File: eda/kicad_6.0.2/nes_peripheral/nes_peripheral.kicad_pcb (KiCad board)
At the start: 2 copper layers, 100 x 100 mm, 119 parts, among them J1 CONN_USER, J10 CONN_JOY2, J11 CONN_JOY2_OE_SEL, J12 CONN_JOY1_OE_SEL, J15 CONN_JOY1_MIC, J16 CONN_5V_RESERVE, J19 CONN_SOUND_IO, J2 CONN_JOY1_FC_COMPATIBLE, J22 CONN_JOY2_MIC, J23 FC_CONN, J24 CONN_CART_DBG, J25 CONN_CART_DBG, J28 CONN_JOY2_DBGSEL, J29 CONN_JOY1_DBGSEL, J3 CONN_JOY2_FC_COMPATIBLE, J30 CONN_GAINSEL, J31 Screw_Terminal_SPK, J32 CONN_SPK, J33 CONN_JOY2_DBG, J34 CONN_JOY1_DBG, J4 Jack_EXT5V, J7 CONN_CART_OE_SEL, J8 CONN_5VSEL, J9 CONN_JOY1, U1 TXB0104PW, U10 TXB0104PW, U11 TXB0104PW, U12 TXB0104PW, U13 TXB0104PW, U14 TXB0104PW, U15 TXB0104PW, U16 TXB0104PW, U17 4021, U18 4021, U19 MAX98357, U2 TXB0104PW, U20 MAX98357, U3 TXB0104PW, U4 TXB0104PW, U5 TXB0104PW, U6 TXB0104PW, U7 TXB0104PW, U8 TXB0104PW, U9 TXB0104PW

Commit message: feat: レベル変換回路配線中
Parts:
- removed J19: CONN_SOUND_IO, Connector_PinSocket_2.54mm:PinSocket_2x03_P2.54mm_Vertical
- C1, C10, C14, C15, C18, C19, C2, C22, C23, C25, C26, C29, C30, C5, C6, C9, J16, J24, J25: moved to B.Cu
- U5: moved to F.Cu
- moved U6 223.4 mm to (96.5, 68.6)
- moved U13 214.4 mm to (96.5, 59.7)
- moved U3 199.0 mm to (83.8, 80.0)
- moved U14 195.0 mm to (96.5, 77.5)
- moved C6 193.0 mm to (85.9, 60.3), turned to 180 degrees
- moved U11 190.2 mm to (83.8, 71.1)
- moved U2 190.1 mm to (83.8, 62.2)
- moved C2 176.8 mm to (81.7, 60.3)
- moved U10 174.2 mm to (109.2, 57.1)
- moved C19 170.8 mm to (81.7, 69.2)
- moved C29 162.6 mm to (98.6, 57.8), turned to 180 degrees
- moved C23 160.4 mm to (85.9, 69.2), turned to 180 degrees
- moved C9 154.6 mm to (94.4, 48.9)
- moved C1 154.4 mm to (107.1, 46.3)
- moved C15 153.9 mm to (98.6, 66.7), turned to 180 degrees
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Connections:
- U14 pad 10: /3V3_~{PA13} -> /5V_~{PA13}
- U15 pad 10: /3V3_PD7 -> /5V_PD7
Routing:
- net GND: track 0.00 -> 1701.2 mm, vias 0 -> 256
- net +5V: track 0.00 -> 74.7 mm, vias 0 -> 8
- net /3V3_A6: track 0.00 -> 73.7 mm, vias 0 -> 2
- net /3V3_A7: track 0.00 -> 72.7 mm, vias 0 -> 2
- net /3V3_D6: track 0.00 -> 71.2 mm, vias 0 -> 2
- net /3V3_D7: track 0.00 -> 70.2 mm, vias 0 -> 2
- net +3V3: track 0.00 -> 70.0 mm, vias 0 -> 8
- net /3V3_A10: track 0.00 -> 67.2 mm
- net /3V3_A11: track 0.00 -> 66.3 mm
- net /5V_D2: track 0.00 -> 65.8 mm
- net /5V_~{WE}: track 0.00 -> 65.1 mm
- net /5V_D3: track 0.00 -> 64.9 mm
- net /3V3_A12: track 0.00 -> 64.6 mm
- net /BOARD_5V: track 0.00 -> 63.9 mm
- net /3V3_O2: track 0.00 -> 63.7 mm
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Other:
- outline, holes or cut-outs redrawn

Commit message: feat: レベル変換回路を引ききった
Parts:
- C11, C12, C16, C17, C20, C24, C27, C3, C31, C4, C7, C8: moved to B.Cu
- moved U12 228.4 mm to (83.8, 88.9)
- moved U8 205.7 mm to (96.5, 104.1)
- moved U7 204.4 mm to (96.5, 86.4)
- moved C3 200.8 mm to (81.7, 78.1)
- moved U15 186.5 mm to (96.5, 95.2)
- moved U4 173.9 mm to (83.8, 97.8)
- moved C16 172.8 mm to (98.6, 84.5), turned to 180 degrees
- moved C27 166.5 mm to (94.5, 93.4)
- moved C24 164.1 mm to (85.9, 87.0), turned to 180 degrees
- moved C11 162.7 mm to (94.5, 84.5)
- moved C8 161.9 mm to (85.9, 95.9), turned to 180 degrees
- moved C4 160.6 mm to (81.8, 95.9)
- moved C20 142.7 mm to (81.7, 87.0)
- moved C17 141.7 mm to (98.6, 102.3), turned to 180 degrees
- moved C31 141.5 mm to (98.6, 93.4), turned to 180 degrees
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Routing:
- net GND: track 1701.2 -> 2673.8 mm, vias 256 -> 322
- net +3V3: track 70.0 -> 182.6 mm, vias 8 -> 14
- net /5V_PA12: track 0.00 -> 70.4 mm
- net /5V_PA11: track 0.00 -> 69.8 mm
- net /5V_PD5: track 0.00 -> 69.2 mm
- net /5V_PD6: track 0.00 -> 68.6 mm
- net /5V_PA8: track 0.00 -> 68.0 mm
- net /CART_OE: track 61.6 -> 129.3 mm, vias 8 -> 14
- net /5V_PA7: track 0.00 -> 67.4 mm
- net +5V: track 74.7 -> 141.3 mm, vias 8 -> 14
- net /3V3_PA5: track 0.00 -> 62.7 mm, vias 0 -> 2
- net /3V3_PA6: track 0.00 -> 62.4 mm, vias 0 -> 2
- net /3V3_PA12: track 0.00 -> 61.3 mm, vias 0 -> 2
- net /3V3_PA1: track 0.00 -> 61.1 mm, vias 0 -> 2
- net /3V3_PA8: track 0.00 -> 60.5 mm, vias 0 -> 2
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
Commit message: feat: 残りの部品配置を修正中
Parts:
- removed J32: CONN_SPK, Resistor_SMD:R_0603_1608Metric_Pad0.98x0.95mm_HandSolder
- J11, J12, J7, J8: footprint Connector_PinSocket_2.54mm:PinSocket_1x03_P2.54mm_Vertical -> Connector_PinHeader_2.54mm:PinHeader_1x03_P2.54mm_Vertical
- J15, J22: footprint Connector_PinSocket_2.54mm:PinSocket_2x01_P2.54mm_Vertical -> Connector_PinSocket_2.54mm:PinSocket_1x02_P2.54mm_Vertical
- J28, J29: footprint Connector_PinSocket_2.54mm:PinSocket_2x01_P2.54mm_Vertical -> Connector_PinHeader_2.54mm:PinHeader_1x02_P2.54mm_Vertical
- J30: footprint Connector_PinSocket_2.54mm:PinSocket_2x05_P2.54mm_Vertical -> Connector_PinHeader_2.54mm:PinHeader_2x05_P2.54mm_Vertical
- J33, J34: footprint Resistor_SMD:R_0603_1608Metric_Pad0.98x0.95mm_HandSolder -> Connector_PinSocket_2.54mm:PinSocket_2x07_P2.54mm_Vertical
- moved U9 238.9 mm to (73.7, 113.0)
- moved U19 225.6 mm to (53.3, 114.3)
- moved U16 222.6 mm to (73.7, 120.7)
- moved J34 221.3 mm to (63.5, 137.2), turned to 90 degrees
- moved D1 215.5 mm to (83.6, 169.8)
- moved C21 215.5 mm to (72.9, 168.3)
- moved R15 215.5 mm to (72.9, 158.7)
- moved D2 215.5 mm to (78.3, 175.1)
- moved U20 212.6 mm to (61.0, 114.3)
- moved R23 204.9 mm to (50.8, 113.0), turned to -90 degrees
- moved U18 202.0 mm to (58.4, 129.5), turned to 90 degrees
- moved C28 201.8 mm to (31.6, 177.1)
- moved C35 201.8 mm to (20.1, 182.8)
- moved C36 201.8 mm to (46.1, 170.2)
- moved R11 201.8 mm to (20.1, 190.3)
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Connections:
- J15 pad 2: Net-(J15-Pad2) -> GND
- J22 pad 2: Net-(J22-Pad2) -> GND
- J33 pad 1: /JOY2_3V3_DBG_D0 -> /JOY2_3V3_DBG_D7
- J34 pad 1: /JOY1_3V3_DBG_D0 -> /JOY1_3V3_DBG_D7
- U16 pad 10: Net-(J22-Pad2) -> /5V_JOY2_MICIN
- U9 pad 10: Net-(J15-Pad2) -> /5V_JOY1_RESERVE
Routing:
- net /BOARD_5V: track 63.9 -> 21.8 mm
- net +3V3: track 182.6 -> 144.6 mm
- net GND: track 2673.8 -> 2675.8 mm, vias 322 -> 326

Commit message: wip: 電源配線中
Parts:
- J33, J34: footprint Connector_PinSocket_2.54mm:PinSocket_2x07_P2.54mm_Vertical -> Connector_PinSocket_2.54mm:PinSocket_2x09_P2.54mm_Vertical
- moved C39 15.8 mm to (62.6, 106.7)
- moved C38 11.0 mm to (62.6, 109.2)
- moved R24 9.24 mm to (57.1, 115.2)
- moved F1 1.04 mm to (106.6, 128.5), turned to -90 degrees
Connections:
- J8 pad 1: /BOARD_5V -> /EXT_5V
- J8 pad 3: /EXT_5V -> /BOARD_5V
- JP1 pad 11: /BOARD_5V -> unconnected-(JP1-Pad11)
- JP1 pad 29: +3V3 -> unconnected-(JP1-Pad29)
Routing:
- net GND: track 2675.8 -> 3019.4 mm, vias 326 -> 402
- net +5V: track 141.3 -> 216.6 mm, vias 14 -> 19
- net /BOARD_5V: track 21.8 -> 90.4 mm, vias 0 -> 4
- net +3V3: track 144.6 -> 207.7 mm, vias 14 -> 18
- net /DAC_I2S_BCLK: track 0.00 -> 34.6 mm, vias 0 -> 1
- net /DAC_I2S_DIN: track 0.00 -> 32.1 mm, vias 0 -> 1
- net /DAC_I2S_LRCLK: track 0.00 -> 31.6 mm, vias 0 -> 1
- net /DAC_~{SD_MODE}: track 0.00 -> 30.2 mm, vias 0 -> 1
- net /GPIO_0_D20: track 0.00 -> 28.1 mm, vias 0 -> 1
- net /GPIO_0_D21: track 0.00 -> 25.6 mm, vias 0 -> 1
- net /CART_OE_IN: track 0.00 -> 25.2 mm, vias 0 -> 1
- net /GPIO_0_D23: track 0.00 -> 23.8 mm, vias 0 -> 1
- net /EXT_5V: track 0.00 -> 15.0 mm, vias 0 -> 2
- net /3V3_PD5: track 55.6 -> 42.0 mm
- net /3V3_PA8: track 60.5 -> 51.2 mm
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
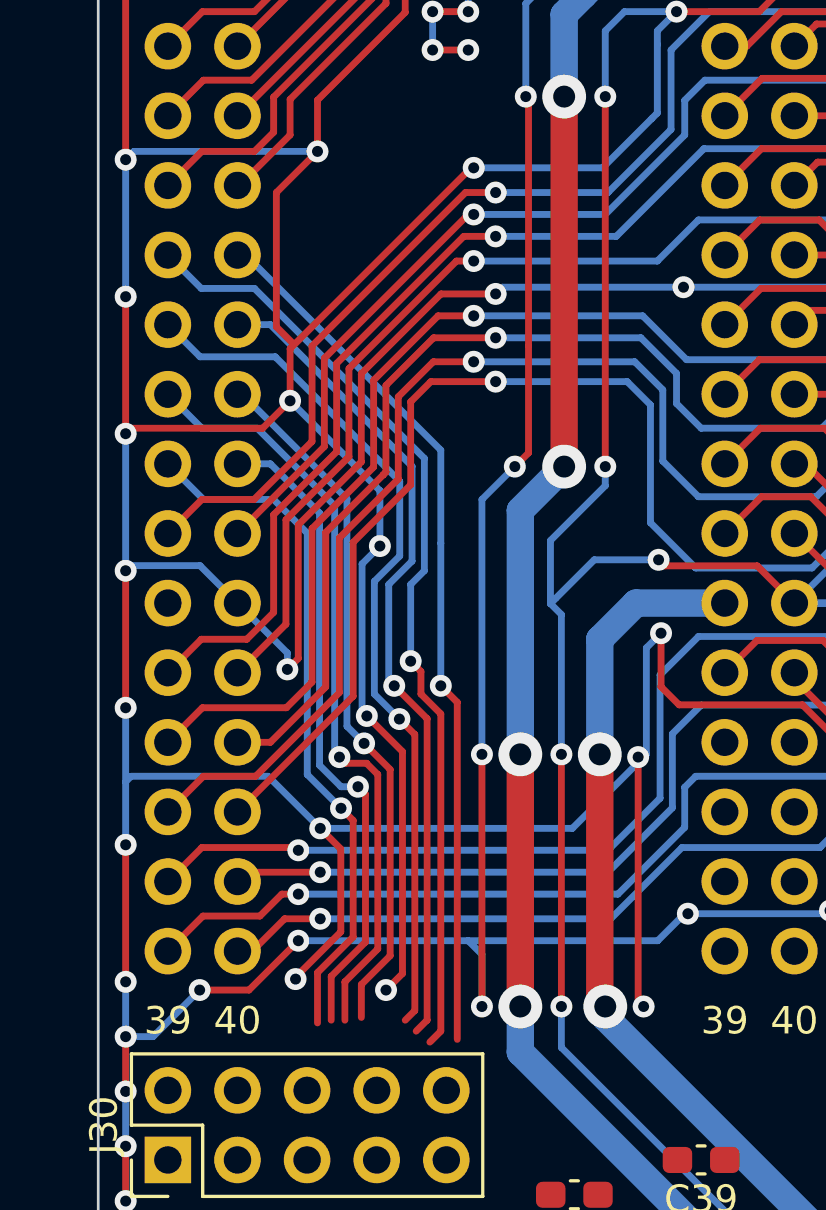
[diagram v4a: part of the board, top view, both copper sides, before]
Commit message: fix: I2Sのピン配置を変更
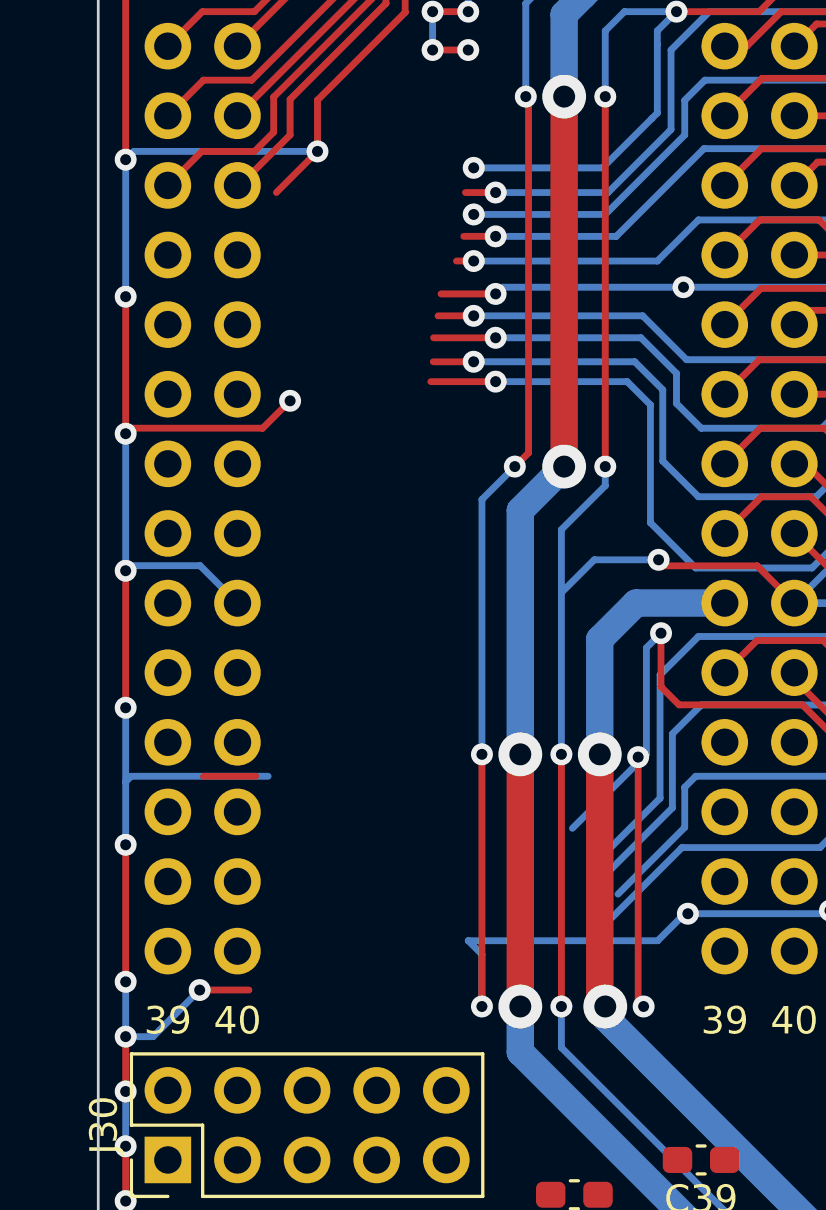
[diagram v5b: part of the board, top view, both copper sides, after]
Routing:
- net GND: track 3019.4 -> 2931.2 mm, vias 402 -> 395
- net /DAC_I2S_BCLK: track 34.6 -> 0.00 mm, vias 1 -> 0
- net /DAC_I2S_DIN: track 32.1 -> 0.30 mm, vias 1 -> 0
- net /DAC_I2S_LRCLK: track 31.6 -> 0.00 mm, vias 1 -> 0
- net /DAC_~{SD_MODE}: track 30.2 -> 0.00 mm, vias 1 -> 0
- net /GPIO_0_D20: track 28.1 -> 0.00 mm, vias 1 -> 0
- net /GPIO_0_D21: track 25.6 -> 0.18 mm, vias 1 -> 0
- net /CART_OE_IN: track 25.2 -> 0.00 mm, vias 1 -> 0
- net /GPIO_0_D23: track 23.8 -> 0.00 mm, vias 1 -> 0
- net /3V3_PA2: track 55.2 -> 33.8 mm
- net /3V3_PA5: track 54.8 -> 33.4 mm
- net /3V3_PA1: track 60.6 -> 40.9 mm
- net /3V3_PA12: track 61.1 -> 42.5 mm
- net /3V3_PA11: track 54.3 -> 35.9 mm
- net /3V3_PA8: track 51.2 -> 32.9 mm
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
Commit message: feat: コントローラの3V3パラレル配線を追加
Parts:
- C35, C36, R10, R11, R12, R13, R14, R15, R16, R17, R18, R19, R20, R21, R22, R7, R8, R9: moved to B.Cu
- J1: footprint Connector_PinSocket_2.54mm:PinSocket_1x06_P2.54mm_Vertical -> Connector_PinSocket_2.54mm:PinSocket_1x04_P2.54mm_Vertical
- J33, J34: footprint Connector_PinSocket_2.54mm:PinSocket_2x09_P2.54mm_Vertical -> Connector_PinSocket_2.54mm:PinSocket_1x09_P2.54mm_Vertical
- moved R11 86.9 mm to (70.9, 119.9), turned to -90 degrees
- moved R7 82.6 mm to (75.0, 129.6), turned to -90 degrees
- moved C35 74.9 mm to (66.7, 124.2), turned to -90 degrees
- moved R20 70.7 mm to (56.7, 119.9), turned to -90 degrees
- moved R17 68.1 mm to (59.2, 129.6), turned to -90 degrees
- moved R21 66.8 mm to (55.2, 119.9), turned to -90 degrees
- moved R10 58.7 mm to (70.5, 129.6), turned to -90 degrees
- moved R13 57.2 mm to (67.9, 119.9), turned to -90 degrees
- moved R9 57.1 mm to (72.0, 129.6), turned to -90 degrees
- moved R14 57.1 mm to (66.6, 129.6), turned to -90 degrees
- moved R18 54.4 mm to (57.7, 129.6), turned to -90 degrees
- moved R12 53.2 mm to (69.4, 119.9), turned to -90 degrees
- moved R22 51.5 mm to (53.9, 129.6), turned to -90 degrees
- moved R16 50.8 mm to (60.7, 129.6), turned to -90 degrees
- moved R8 46.7 mm to (73.5, 129.6), turned to -90 degrees
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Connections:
- D3 pad 2: /GPIO_0_D23 -> /USER_LED
- J1 pad 3: /GPIO_0_D20 -> /GPIO_1_D34
- J1 pad 4: /GPIO_0_D21 -> /GPIO_1_D35
- J10 pad 2: /3V3_JOY2_DO -> /GPIO_1_D29
- J10 pad 3: /3V3_JOY2_P/~{S} -> /GPIO_1_D30
- J10 pad 4: /3V3_JOY2_CLK -> /GPIO_1_D31
- J10 pad 5: /3V3_JOY2_MICIN -> /GPIO_1_D28
- J28 pad 2: /3V3_JOY2_DO -> /GPIO_1_D29
- J29 pad 2: /3V3_JOY1_DO -> /GPIO_0_D29
- J33 pad 2: GND -> /JOY2_3V3_DBG_D6
- J33 pad 3: /JOY2_3V3_DBG_D6 -> /JOY2_3V3_DBG_D5
- J33 pad 4: GND -> /JOY2_3V3_DBG_D4
- J33 pad 5: /JOY2_3V3_DBG_D5 -> /JOY2_3V3_DBG_D3
- J33 pad 6: GND -> /JOY2_3V3_DBG_D2
- J33 pad 7: /JOY2_3V3_DBG_D4 -> /JOY2_3V3_DBG_D1
- J33 pad 8: GND -> /JOY2_3V3_DBG_D0
- J33 pad 9: /JOY2_3V3_DBG_D3 -> GND
- J34 pad 2: GND -> /JOY1_3V3_DBG_D6
- J34 pad 3: /JOY1_3V3_DBG_D6 -> /JOY1_3V3_DBG_D5
- J34 pad 4: GND -> /JOY1_3V3_DBG_D4
- J34 pad 5: /JOY1_3V3_DBG_D5 -> /JOY1_3V3_DBG_D3
- J34 pad 6: GND -> /JOY1_3V3_DBG_D2
- J34 pad 7: /JOY1_3V3_DBG_D4 -> /JOY1_3V3_DBG_D1
- J34 pad 8: GND -> /JOY1_3V3_DBG_D0
- J34 pad 9: /JOY1_3V3_DBG_D3 -> GND
- J7 pad 3: /CART_OE_IN -> /GPIO_1_D33
- J9 pad 2: /3V3_JOY1_DO -> /GPIO_0_D29
- J9 pad 3: /3V3_JOY1_P/~{S} -> /GPIO_0_D30
- J9 pad 4: /3V3_JOY1_CLK -> /GPIO_0_D31
- J9 pad 5: /3V3_JOY1_RESERVE -> /GPIO_0_D28
- JP1 pad 19: /DAC_I2S_BCLK -> /GPIO_0_D16
- JP1 pad 20: /DAC_I2S_DIN -> /GPIO_0_D17
- JP1 pad 21: /DAC_I2S_LRCLK -> /GPIO_0_D18
- JP1 pad 22: /DAC_~{SD_MODE} -> /GPIO_0_D19
- JP1 pad 25: /CART_OE_IN -> /3V3_PA1
- JP1 pad 27: /3V3_PA6 -> /3V3_PD1
- JP1 pad 28: /3V3_PA7 -> /GPIO_0_D25
- JP1 pad 31: /3V3_PA5 -> /GPIO_0_D26
- JP1 pad 32: /3V3_PA8 -> /GPIO_0_D27
- JP1 pad 33: /3V3_PA2 -> /GPIO_0_D28
- JP1 pad 34: /3V3_PA11 -> /GPIO_0_D29
- JP1 pad 35: /3V3_PA1 -> /GPIO_0_D30
- JP1 pad 36: /3V3_PA12 -> /GPIO_0_D31
- JP1 pad 37: /3V3_PD1 -> /GPIO_0_D32
- JP1 pad 38: /3V3_PD6 -> /GPIO_0_D33
- JP1 pad 39: /3V3_PD2 -> /GPIO_0_D34
- JP1 pad 40: /3V3_PD5 -> /GPIO_0_D35
- JP2 pad 33: /3V3_JOY1_RESERVE -> /GPIO_1_D28
- JP2 pad 34: /3V3_JOY2_MICIN -> /GPIO_1_D29
- JP2 pad 35: /3V3_JOY1_DO -> /GPIO_1_D30
- JP2 pad 36: /3V3_JOY2_DO -> /GPIO_1_D31
- JP2 pad 37: /3V3_JOY1_P/~{S} -> /USER_LED
- JP2 pad 38: /3V3_JOY2_P/~{S} -> /GPIO_1_D33
- JP2 pad 39: /3V3_JOY1_CLK -> /GPIO_1_D34
- JP2 pad 40: /3V3_JOY2_CLK -> /GPIO_1_D35
- R23 pad 2: /DAC_~{SD_MODE} -> /GPIO_0_D35
- R24 pad 2: /DAC_~{SD_MODE} -> /GPIO_0_D35
- U12 pad 2: /3V3_PA2 -> /GPIO_0_D20
- U12 pad 3: /3V3_PA11 -> /GPIO_0_D21
- U12 pad 5: /3V3_PA12 -> /GPIO_0_D23
- U16 pad 2: /3V3_JOY2_DO -> /GPIO_1_D29
- U16 pad 3: /3V3_JOY2_P/~{S} -> /GPIO_1_D30
- U16 pad 4: /3V3_JOY2_CLK -> /GPIO_1_D31
- U16 pad 5: /3V3_JOY2_MICIN -> /GPIO_1_D28
- U17 pad 10: /3V3_JOY2_CLK -> /GPIO_1_D31
- U17 pad 9: /3V3_JOY2_P/~{S} -> /GPIO_1_D30
- U18 pad 10: /3V3_JOY1_CLK -> /GPIO_0_D31
- U18 pad 9: /3V3_JOY1_P/~{S} -> /GPIO_0_D30
- U19 pad 1: /DAC_I2S_DIN -> /GPIO_0_D33
- U19 pad 12: (no net) -> unconnected-(U19-Pad12)
- U19 pad 13: (no net) -> unconnected-(U19-Pad13)
- U19 pad 14: /DAC_I2S_LRCLK -> /GPIO_0_D34
- U19 pad 16: /DAC_I2S_BCLK -> /GPIO_0_D32
- U19 pad 5: (no net) -> unconnected-(U19-Pad5)
- U19 pad 6: (no net) -> unconnected-(U19-Pad6)
- U20 pad 1: /DAC_I2S_DIN -> /GPIO_0_D33
- U20 pad 12: (no net) -> unconnected-(U20-Pad12)
- U20 pad 13: (no net) -> unconnected-(U20-Pad13)
- U20 pad 14: /DAC_I2S_LRCLK -> /GPIO_0_D34
- U20 pad 16: /DAC_I2S_BCLK -> /GPIO_0_D32
- U20 pad 5: (no net) -> unconnected-(U20-Pad5)
- U20 pad 6: (no net) -> unconnected-(U20-Pad6)
- U3 pad 2: /3V3_PA6 -> /GPIO_0_D16
- U3 pad 3: /3V3_PA7 -> /GPIO_0_D17
- U3 pad 4: /3V3_PA5 -> /GPIO_0_D18
- U3 pad 5: /3V3_PA8 -> /GPIO_0_D19
- U4 pad 3: /3V3_PD6 -> /GPIO_0_D25
- U4 pad 4: /3V3_PD2 -> /GPIO_0_D26
- U4 pad 5: /3V3_PD5 -> /GPIO_0_D27
- U9 pad 2: /3V3_JOY1_DO -> /GPIO_0_D29
- U9 pad 3: /3V3_JOY1_P/~{S} -> /GPIO_0_D30
- U9 pad 4: /3V3_JOY1_CLK -> /GPIO_0_D31
- U9 pad 5: /3V3_JOY1_RESERVE -> /GPIO_0_D28
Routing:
- net GND: track 2931.2 -> 3148.9 mm, vias 395 -> 431
- net +3V3: track 207.7 -> 262.3 mm, vias 18 -> 25
- net /GPIO_0_D23: track 0.00 -> 52.5 mm, vias 0 -> 2
- net /GPIO_0_D16: track 0.00 -> 50.9 mm, vias 0 -> 2
- net /GPIO_0_D18: track 0.00 -> 45.6 mm, vias 0 -> 2
- net /GPIO_0_D26: track 0.00 -> 45.4 mm, vias 0 -> 2
- net /GPIO_0_D20: track 0.00 -> 45.3 mm, vias 0 -> 2
- net /GPIO_0_D17: track 0.00 -> 44.9 mm, vias 0 -> 2
- net /GPIO_0_D21: track 0.18 -> 44.9 mm, vias 0 -> 2
- net /GPIO_0_D27: track 0.00 -> 43.1 mm, vias 0 -> 2
- net /3V3_PA12: track 42.5 -> 0.00 mm, vias 2 -> 0
- net /GPIO_0_D25: track 0.00 -> 42.2 mm, vias 0 -> 2
- net /GPIO_0_D19: track 0.00 -> 41.9 mm, vias 0 -> 2
- net /3V3_PA6: track 39.1 -> 0.00 mm, vias 2 -> 0
- net /JOY2_3V3_DBG_D4: track 0.00 -> 37.4 mm, vias 0 -> 2
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
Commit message: feat: 音声出力回路をモノラルに変更、配線を修正
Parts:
- removed C38: 0.1u, Capacitor_SMD:C_0603_1608Metric_Pad1.08x0.95mm_HandSolder
- removed C39: 10p, Capacitor_SMD:C_0603_1608Metric_Pad1.08x0.95mm_HandSolder
- removed R24: 330k, Resistor_SMD:R_0603_1608Metric_Pad0.98x0.95mm_HandSolder
- removed U20: MAX98357, nes_peripheral:QFN-16_EP_3x3_Pitch0.5mm
- C13, C21, C37, C40, R23, R25: moved to B.Cu
- J11, J12: footprint Connector_PinHeader_2.54mm:PinHeader_1x03_P2.54mm_Vertical -> Connector_PinHeader_2.54mm:PinHeader_1x02_P2.54mm_Vertical
- J30: footprint Connector_PinHeader_2.54mm:PinHeader_2x05_P2.54mm_Vertical -> Connector_PinHeader_2.54mm:PinHeader_2x03_P2.54mm_Vertical
- J31: footprint TerminalBlock:TerminalBlock_bornier-4_P5.08mm -> TerminalBlock:TerminalBlock_bornier-2_P5.08mm
- moved D3 145.0 mm to (74.9, 102.3), turned to 90 degrees
- moved R26 82.0 mm to (44.2, 101.9), turned to 180 degrees
- moved C13 81.9 mm to (62.8, 110.7), turned to -90 degrees
- moved R25 73.4 mm to (44.2, 101.9)
- moved R3 67.2 mm to (74.9, 106.1), turned to -90 degrees
- moved C21 54.4 mm to (62.8, 114.9), turned to 90 degrees
- moved J12 34.5 mm to (55.9, 111.8), turned to 0 degrees
- moved J15 30.9 mm to (53.3, 111.8)
- moved J29 16.3 mm to (83.1, 110.7), turned to 90 degrees
- moved C40 13.7 mm to (44.5, 110.1), turned to 0 degrees
- moved U9 10.3 mm to (61.0, 112.8)
- moved C37 9.83 mm to (44.5, 111.8), turned to 0 degrees
- moved J1 8.03 mm to (71.1, 106.7), turned to 180 degrees
- moved J31 7.62 mm to (45.7, 121.9)
- moved U19 7.62 mm to (45.7, 114.3), turned to -90 degrees
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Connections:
- net /GPIO_0_D16 renamed /3V3_PA6
- net /GPIO_0_D17 renamed /3V3_PA7
- net /GPIO_0_D18 renamed /3V3_PA5
- net /GPIO_0_D19 renamed /3V3_PA8
- net /GPIO_0_D20 renamed /3V3_PA2
- net /GPIO_0_D21 renamed /3V3_PA11
- net /GPIO_0_D23 renamed /3V3_PA12
- net /GPIO_0_D25 renamed /3V3_PD6
- net /GPIO_0_D26 renamed /3V3_PD2
- net /GPIO_0_D27 renamed /3V3_PD5
- net /GPIO_0_D29 renamed /3V3_JOY1_DO
- net /GPIO_0_D31 renamed /3V3_JOY1_CLK
- net /GPIO_0_D32 renamed /DAC_I2S_BCLK
- net /SPK_OUT_L_N renamed /SPK_OUT_N
- net /SPK_OUT_L_P renamed /SPK_OUT_P
- D3 pad 2: /USER_LED -> /GPIO_1_D29
- J1 pad 3: /GPIO_1_D34 -> /GPIO_1_D28
- J1 pad 4: /GPIO_1_D35 -> /GPIO_1_D31
- J10 pad 2: /GPIO_1_D29 -> /3V3_JOY2_DO
- J10 pad 3: /GPIO_1_D30 -> /3V3_JOY2_P/~{S}
- J10 pad 4: /GPIO_1_D31 -> /3V3_JOY2_CLK
- J10 pad 5: /GPIO_1_D28 -> /3V3_JOY2_MICIN
- J28 pad 2: /GPIO_1_D29 -> /3V3_JOY2_DO
- J30 pad 1: /GAIN_SLOT -> GND
- J30 pad 4: GND -> /GAIN_SLOT
- J30 pad 5: /GAIN_SLOT -> Net-(J30-Pad5)
- J30 pad 6: unconnected-(J30-Pad6) -> +3V3
- J7 pad 3: /GPIO_1_D33 -> /GPIO_1_D35
- J9 pad 3: /GPIO_0_D30 -> /3V3_JOY1_P/~{S}
- J9 pad 5: /GPIO_0_D28 -> /3V3_JOY1_RESERVE
- JP1 pad 33: /GPIO_0_D28 -> /3V3_JOY1_P/~{S}
- JP1 pad 35: /GPIO_0_D30 -> /3V3_JOY1_RESERVE
- JP1 pad 38: /GPIO_0_D33 -> /DAC_I2S_LRCLK
- JP1 pad 39: /GPIO_0_D34 -> /DAC_~{SD_MODE}
- JP1 pad 40: /GPIO_0_D35 -> /DAC_I2S_DIN
- JP2 pad 35: /GPIO_1_D30 -> /3V3_JOY2_DO
- JP2 pad 37: /USER_LED -> /3V3_JOY2_MICIN
- JP2 pad 38: /GPIO_1_D33 -> /3V3_JOY2_CLK
- JP2 pad 39: /GPIO_1_D34 -> /3V3_JOY2_P/~{S}
- R23 pad 2: /GPIO_0_D35 -> /DAC_~{SD_MODE}
- R26 pad 1: GND -> Net-(J30-Pad5)
- R26 pad 2: Net-(J30-Pad10) -> GND
- U16 pad 2: /GPIO_1_D29 -> /3V3_JOY2_DO
- U16 pad 3: /GPIO_1_D30 -> /3V3_JOY2_P/~{S}
- U16 pad 4: /GPIO_1_D31 -> /3V3_JOY2_CLK
- U16 pad 5: /GPIO_1_D28 -> /3V3_JOY2_MICIN
- U17 pad 10: /GPIO_1_D31 -> /3V3_JOY2_CLK
- U17 pad 9: /GPIO_1_D30 -> /3V3_JOY2_P/~{S}
- U18 pad 9: /GPIO_0_D30 -> /3V3_JOY1_P/~{S}
- U19 pad 1: /GPIO_0_D33 -> /DAC_I2S_DIN
- U19 pad 14: /GPIO_0_D34 -> /DAC_I2S_LRCLK
- U9 pad 3: /GPIO_0_D30 -> /3V3_JOY1_P/~{S}
- U9 pad 5: /GPIO_0_D28 -> /3V3_JOY1_RESERVE
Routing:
- net GND: track 3148.9 -> 3236.3 mm, vias 431 -> 458
- net /BOARD_5V: track 85.6 -> 46.8 mm
- net /3V3_JOY1_P/~{S}: track 0.00 -> 32.0 mm
- net /3V3_JOY1_DO: track 0.00 -> 28.5 mm
- net /3V3_JOY1_RESERVE: track 0.00 -> 27.6 mm
- net /DAC_I2S_BCLK: track 0.00 -> 24.1 mm
- net /DAC_I2S_LRCLK: track 0.00 -> 23.1 mm
- net /DAC_I2S_DIN: track 0.00 -> 20.6 mm
- net /DAC_~{SD_MODE}: track 0.00 -> 19.2 mm, vias 0 -> 1
- net /SPK_OUT_N: track 0.00 -> 16.6 mm
- net /SPK_OUT_P: track 0.00 -> 16.2 mm
- net /GPIO_1_D28: track 0.00 -> 16.0 mm
- net /3V3_JOY1_CLK: track 13.2 -> 27.5 mm
- net /GPIO_1_D29: track 0.00 -> 14.1 mm
- net +5V: track 209.0 -> 223.0 mm, vias 18 -> 19
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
